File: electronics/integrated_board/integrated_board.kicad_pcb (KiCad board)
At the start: 2 copper layers, 54 parts, among them CON1 BARREL_JACK, J1 Conn_01x04_Female, J13 Conn_01x05_Female, J15 Conn_01x05_Female, J17 Conn_01x05_Female, J2 Conn_01x04_Female, J3 Conn_01x04_Female, P10 Conn_01x02, P15 Conn_01x02, P16 UART, P2 A1, P3 A2, P4 A3, P5 I2C 2, U3 LM2596T-5, U4 ESP32-DEVKITC-32D, U5 ULN2003, U6 ULN2003

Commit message: update integrated board
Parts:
- removed C10: 22nF, Capacitor_THT:CP_Radial_D4.0mm_P2.00mm
- removed J3: Conn_01x04_Female, Connector_JST:JST_XH_B4B-XH-A_1x04_P2.50mm_Vertical
- removed P5: I2C 2, Connector_JST:JST_XH_B4B-XH-A_1x04_P2.50mm_Vertical
- removed R16, R17: 1k, Resistor_THT:R_Axial_DIN0309_L9.0mm_D3.2mm_P12.70mm_Horizontal
- removed R18, R19: 1.8k, Resistor_THT:R_Axial_DIN0309_L9.0mm_D3.2mm_P12.70mm_Horizontal
- removed U5, U6: ULN2003, Package_DIP:DIP-16_W7.62mm_Socket_LongPads
- added C13: 22nF, Capacitor_THT:CP_Radial_D4.0mm_P2.00mm, F.Cu at (170.1, 106.8)
- added J5: to_rotary_encoder2 (14,27), Connector_JST:JST_XH_B4B-XH-A_1x04_P2.50mm_Vertical, F.Cu at (188.7, 100.5)
- added P1: Conn_01x02, Connector_JST:JST_XH_B2B-XH-A_1x02_P2.50mm_Vertical, F.Cu at (110.7, 49.8)
- added P6: io, Connector_JST:JST_XH_B4B-XH-A_1x04_P2.50mm_Vertical, F.Cu at (98.2, 130.8)
- added Q1: 2N7000, Package_TO_SOT_THT:TO-92_Inline_Wide, F.Cu at (163.4, 49.7)
- added Q2: 2N7000, Package_TO_SOT_THT:TO-92_Inline_Wide, F.Cu at (163.6, 67.3)
- added Q3: 2N7000, Package_TO_SOT_THT:TO-92_Inline_Wide, F.Cu at (163.4, 137.8)
- added Q4: 2N7000, Package_TO_SOT_THT:TO-92_Inline_Wide, F.Cu at (163.4, 120.4)
- added Q5: 2N7000, Package_TO_SOT_THT:TO-92_Inline_Wide, F.Cu at (163.7, 103.0)
- added Q6: 2N7000, Package_TO_SOT_THT:TO-92_Inline_Wide, F.Cu at (163.8, 85.0)
- added R28: 1k, Resistor_THT:R_Axial_DIN0309_L9.0mm_D3.2mm_P12.70mm_Horizontal, F.Cu at (179.9, 111.5)
- added R29: 1k, Resistor_THT:R_Axial_DIN0411_L9.9mm_D3.6mm_P12.70mm_Horizontal, F.Cu at (175.8, 111.5)
- added R30: 1k, Resistor_THT:R_Axial_DIN0411_L9.9mm_D3.6mm_P12.70mm_Horizontal, F.Cu at (175.8, 99.3)
- added R31: 1k, Resistor_THT:R_Axial_DIN0309_L9.0mm_D3.2mm_P12.70mm_Horizontal, F.Cu at (179.9, 81.7)
- added U1: ULN2003, Package_DIP:DIP-16_W7.62mm_LongPads, F.Cu at (123.0, 102.8)
- added U2: ULN2003, Package_DIP:DIP-16_W7.62mm_LongPads, F.Cu at (123.0, 80.4)
- C3, C4: value 22nF -> C_Small; footprint Capacitor_THT:CP_Radial_D4.0mm_P2.00mm -> Capacitor_THT:C_Disc_D6.0mm_W4.4mm_P5.00mm
- C7, C8: value C_Small -> 22nF; footprint Capacitor_THT:C_Disc_D6.0mm_W4.4mm_P5.00mm -> Capacitor_THT:CP_Radial_D4.0mm_P2.00mm
- J1: value Conn_01x04_Female -> to_rotary_encoder3(12,13)
- J13: value Conn_01x05_Female -> to_motor1(2,15,16,17)
- J15: value Conn_01x05_Female -> to_motor2 (5,18,19,21)
- J17: value Conn_01x05_Female -> to_motor3 (22,23,9,10)
- J2: value Conn_01x04_Female -> to_rotary_encoder3
- P2: value A1 -> io
- P4: value A3 -> io
- R1, R10, R11, R2, R3, R4, R8, R9: footprint Resistor_THT:R_Axial_DIN0309_L9.0mm_D3.2mm_P12.70mm_Horizontal -> Resistor_THT:R_Axial_DIN0411_L9.9mm_D3.6mm_P12.70mm_Horizontal
- R12, R13: value 1.8k -> 1k; footprint Resistor_THT:R_Axial_DIN0309_L9.0mm_D3.2mm_P12.70mm_Horizontal -> Resistor_THT:R_Axial_DIN0411_L9.9mm_D3.6mm_P12.70mm_Horizontal
- R5, R6: value 1.8k -> 1k
- moved P3 180.4 mm to (117.2, 130.8), turned to -90 degrees
- moved P4 172.3 mm to (117.2, 116.2), turned to -90 degrees
- moved P2 167.1 mm to (107.5, 130.8), turned to -90 degrees
- moved C9 165.6 mm to (170.3, 123.3), turned to 90 degrees
- moved C1 163.8 mm to (170.4, 53.0), turned to 90 degrees
- moved C2 162.9 mm to (170.4, 71.0), turned to 90 degrees
- moved J1 161.4 mm to (188.7, 66.0), turned to 90 degrees
- moved R5 155.1 mm to (179.7, 46.3), turned to -90 degrees
- moved J2 153.9 mm to (188.7, 137.0), turned to 90 degrees
- moved R6 150.6 mm to (179.7, 76.7), turned to 90 degrees
- moved R15 150.4 mm to (179.7, 117.3), turned to -90 degrees
- moved R14 150.3 mm to (179.7, 134.3), turned to -90 degrees
- moved H1 149.5 mm to (189.2, 45.5)
- moved R12 149.4 mm to (175.7, 146.7), turned to 180 degrees
- moved R10 148.7 mm to (175.6, 134.2), turned to 180 degrees
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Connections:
- C1 pad 1: GND -> Net-(J1-Pin_2)
- C1 pad 2: Net-(J1-Pin_1) -> GND
- C2 pad 1: GND -> Net-(J1-Pin_1)
- C2 pad 2: Net-(J1-Pin_2) -> GND
- C3 pad 2: Net-(J2-Pin_1) -> +5V
- C4 pad 2: Net-(J2-Pin_2) -> +5V
- C5 pad 1: Net-(P10-Pin_1) -> Net-(P1-Pin_2)
- C7 pad 1: GND -> Net-(J5-Pin_2)
- C7 pad 2: +5V -> GND
- C8 pad 1: GND -> Net-(J2-Pin_1)
- C8 pad 2: +5V -> GND
- C9 pad 1: GND -> Net-(J2-Pin_2)
- C9 pad 2: Net-(J3-Pin_1) -> GND
- CON1 pad 1: Net-(P10-Pin_1) -> Net-(P1-Pin_1)
- P10 pad 1: Net-(P10-Pin_1) -> Net-(P1-Pin_2)
- P15 pad 1: Net-(P10-Pin_1) -> Net-(P1-Pin_2)
- P2 pad 1: A1-3 -> Net-(P2-Pin_1)
- P2 pad 2: A1-4 -> Net-(P2-Pin_2)
- P4 pad 1: A3-3 -> Net-(P4-Pin_1)
- P4 pad 2: A3-4 -> Net-(P4-Pin_2)
- R1 pad 1: Net-(J1-Pin_1) -> +3V3
- R1 pad 2: +5V -> Net-(Q1-S)
- R10 pad 1: D5-3 -> +3V3
- R10 pad 2: Net-(J2-Pin_1) -> Net-(Q3-S)
- R11 pad 1: D5-4 -> +3V3
- R11 pad 2: Net-(J2-Pin_2) -> Net-(Q4-S)
- R12 pad 1: GND -> +5V
- R12 pad 2: D5-3 -> Net-(J2-Pin_1)
- R13 pad 1: GND -> +5V
- R13 pad 2: D5-4 -> Net-(J2-Pin_2)
- R14 pad 1: Net-(J3-Pin_1) -> Net-(J2-Pin_1)
- R15 pad 1: Net-(J3-Pin_2) -> +5V
- R15 pad 2: +5V -> Net-(J2-Pin_2)
- R2 pad 1: Net-(J1-Pin_2) -> +3V3
- R2 pad 2: +5V -> Net-(Q2-S)
- R3 pad 1: D1-3 -> +5V
- R3 pad 2: Net-(J1-Pin_1) -> Net-(J1-Pin_2)
- R4 pad 1: D1-4 -> +5V
- R4 pad 2: Net-(J1-Pin_2) -> Net-(J1-Pin_1)
- R5 pad 1: GND -> Net-(J1-Pin_2)
- R5 pad 2: D1-3 -> +5V
- R6 pad 1: GND -> +5V
- R6 pad 2: D1-4 -> Net-(J1-Pin_1)
- R7 pad 2: Net-(P10-Pin_1) -> Net-(P1-Pin_2)
- R8 pad 1: Net-(J2-Pin_1) -> +3V3
- R8 pad 2: +5V -> Net-(Q6-S)
- R9 pad 1: Net-(J2-Pin_2) -> +5V
- R9 pad 2: +5V -> Net-(J5-Pin_2)
- U3 pad 1: Net-(P10-Pin_1) -> Net-(P1-Pin_2)
- U4 pad 1: unconnected-(U4-3V3-Pad1) -> +3V3
- U4 pad 10: D8-3 -> Net-(Q4-S)
- U4 pad 11: D7-4 -> Net-(Q5-S)
- U4 pad 12: D7-3 -> Net-(Q6-S)
- U4 pad 13: I2C_2-3 -> Net-(Q2-S)
- U4 pad 15: I2C_2-4 -> Net-(Q1-S)
- U4 pad 16: I2C_1-3 -> to_uln2003_2
- U4 pad 17: I2C_1-4 -> to_uln2003_1
- U4 pad 21: D6-4 -> Net-(U1-I5)
- U4 pad 22: D6-3 -> Net-(U1-I6)
- U4 pad 25: D5-4 -> Net-(U1-I7)
- U4 pad 27: D5-3 -> Net-(U2-I1)
- U4 pad 28: D4-4 -> Net-(U2-I2)
- U4 pad 29: D4-3 -> Net-(U2-I3)
- U4 pad 30: D3-4 -> Net-(U2-I4)
- U4 pad 31: D3-3 -> Net-(U2-I5)
- U4 pad 32: D2-4 -> Net-(P6-Pin_1)
- U4 pad 33: D2-3 -> Net-(P6-Pin_2)
- U4 pad 34: D1-4 -> Net-(U2-I6)
- U4 pad 35: D1-3 -> Net-(U2-I7)
- U4 pad 5: A1-4 -> Net-(P4-Pin_2)
- U4 pad 6: A1-3 -> Net-(P4-Pin_1)
- U4 pad 7: A3-3 -> Net-(P2-Pin_2)
- U4 pad 8: A3-4 -> Net-(P2-Pin_1)
- U4 pad 9: D8-4 -> Net-(Q3-S)
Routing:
- net +5V: track 0.00 -> 571.4 mm
- net +3V3: track 0.00 -> 219.7 mm
- net Net-(P1-Pin_2): track 0.00 -> 177.9 mm
- net Net-(P6-Pin_2): track 0.00 -> 99.1 mm
- net Net-(P6-Pin_1): track 0.00 -> 93.8 mm
- net Net-(P2-Pin_2): track 0.00 -> 82.3 mm
- net Net-(P2-Pin_1): track 0.00 -> 81.3 mm
- net Net-(Q3-S): track 0.00 -> 72.0 mm
- net A2-4: track 0.00 -> 69.5 mm
- net A2-3: track 0.00 -> 68.6 mm
- net to_uln2003_1: track 0.00 -> 66.9 mm
- net to_uln2003_2: track 0.00 -> 65.9 mm
- net RX: track 0.00 -> 63.8 mm
- net TX: track 0.00 -> 59.9 mm
- net Net-(P4-Pin_2): track 0.00 -> 58.1 mm
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- added copper zone on B.Cu, net GND
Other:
- board outline added: 98.5 x 111 mm
- board text added: "12V"
- board text added: "12V conn"
- board text added: "Antenna side"
- board text added: "GND"
- board text added: "IO0"
- board text added: "IO34"
- board text added: "IO35"
- board text added: "IO36"
- board text added: "IO39"
- board text added: "IO4"
- board text added: "RX"
- board text added: "TX"
- board text added: "USB side"
- board text added: "VCC"
- board text added: "based on BeeHive v0.7"
- board text added: "board by Andre Maia Chagas licensed under CERN-OHL-W 2.0 https://ohwr.org/project/cernohl"

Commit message: update integrated board
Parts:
- removed P3: A2, Connector_JST:JST_XH_B4B-XH-A_1x04_P2.50mm_Vertical
- removed P6: io, Connector_JST:JST_XH_B4B-XH-A_1x04_P2.50mm_Vertical
- added R16: 10k, Resistor_THT:R_Axial_DIN0411_L9.9mm_D3.6mm_P12.70mm_Horizontal, F.Cu at (63.8, 75.8)
- added R17: 10k, Resistor_THT:R_Axial_DIN0411_L9.9mm_D3.6mm_P12.70mm_Horizontal, F.Cu at (63.8, 80.9)
- added R18: 1k, Resistor_THT:R_Axial_DIN0411_L9.9mm_D3.6mm_P12.70mm_Horizontal, F.Cu at (63.8, 86.0)
- added R19: 1k, Resistor_THT:R_Axial_DIN0411_L9.9mm_D3.6mm_P12.70mm_Horizontal, F.Cu at (63.8, 91.2)
- added R20: 1k, Resistor_THT:R_Axial_DIN0411_L9.9mm_D3.6mm_P12.70mm_Horizontal, F.Cu at (63.8, 96.3)
- added R21: 1k, Resistor_THT:R_Axial_DIN0411_L9.9mm_D3.6mm_P12.70mm_Horizontal, F.Cu at (63.8, 101.5)
- added SW1: SW_Push, Connector_JST:JST_XH_B2B-XH-A_1x02_P2.50mm_Vertical, F.Cu at (82.0, 76.5)
- added SW2: SW_Push, Connector_JST:JST_XH_B2B-XH-A_1x02_P2.50mm_Vertical, F.Cu at (82.0, 84.3)
- J13: value to_motor1(2,15,16,17) -> to_motor1(15,2,0,4)
- J15: value to_motor2 (5,18,19,21) -> to_motor2 (16,17,5,18)
- J17: value to_motor3 (22,23,9,10) -> to_motor3 (19,21,22,23)
- P2: value io -> LCD
- moved P2 9.20 mm to (98.2, 130.8)
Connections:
- net Net-(Q5-S) renamed encoderX_2
- net Net-(Q6-S) renamed encoderX_1
- Q1 pad 1: Net-(Q1-S) -> encoderZ_1
- Q2 pad 1: Net-(Q2-S) -> encoderZ_2
- Q3 pad 1: Net-(Q3-S) -> encoderY_1
- Q4 pad 1: Net-(Q4-S) -> encoderY_2
- R1 pad 2: Net-(Q1-S) -> encoderZ_1
- R10 pad 2: Net-(Q3-S) -> encoderY_1
- R11 pad 2: Net-(Q4-S) -> encoderY_2
- R2 pad 2: Net-(Q2-S) -> encoderZ_2
- U1 pad 3: to_uln2003_2 -> Net-(U1-I3)
- U1 pad 4: to_uln2003_1 -> Net-(U1-I4)
- U4 pad 10: Net-(Q4-S) -> encoderY_1
- U4 pad 13: Net-(Q2-S) -> Net-(P4-Pin_2)
- U4 pad 15: Net-(Q1-S) -> Net-(P4-Pin_1)
- U4 pad 16: to_uln2003_2 -> unconnected-(U4-SD2-Pad16)
- U4 pad 17: to_uln2003_1 -> unconnected-(U4-SD3-Pad17)
- U4 pad 21: Net-(U1-I5) -> Net-(U1-I3)
- U4 pad 22: Net-(U1-I6) -> Net-(U1-I4)
- U4 pad 25: Net-(U1-I7) -> Net-(U1-I5)
- U4 pad 27: Net-(U2-I1) -> Net-(U1-I6)
- U4 pad 28: Net-(U2-I2) -> Net-(U1-I7)
- U4 pad 29: Net-(U2-I3) -> Net-(U2-I1)
- U4 pad 3: A2-4 -> switch2
- U4 pad 30: Net-(U2-I4) -> Net-(U2-I2)
- U4 pad 31: Net-(U2-I5) -> Net-(U2-I3)
- U4 pad 32: Net-(P6-Pin_1) -> Net-(U2-I4)
- U4 pad 33: Net-(P6-Pin_2) -> Net-(U2-I5)
- U4 pad 4: A2-3 -> switch1
- U4 pad 5: Net-(P4-Pin_2) -> encoderZ_2
- U4 pad 6: Net-(P4-Pin_1) -> encoderZ_1
- U4 pad 9: Net-(Q3-S) -> encoderY_2
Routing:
- net (no net): track 0.00 -> 132.8 mm
- net Net-(P6-Pin_2): track 99.1 -> 0.00 mm
- net Net-(P6-Pin_1): track 93.8 -> 0.00 mm
- net Net-(Q3-S): track 72.0 -> 0.00 mm
- net A2-4: track 69.5 -> 0.00 mm
- net A2-3: track 68.6 -> 0.00 mm
- net to_uln2003_1: track 66.9 -> 0.00 mm
- net to_uln2003_2: track 65.9 -> 0.00 mm
- net Net-(Q4-S): track 56.6 -> 0.00 mm
- net switch1: track 0.00 -> 20.7 mm
- net switch2: track 0.00 -> 19.2 mm
- net Net-(Q1-S): track 16.1 -> 0.00 mm
- net Net-(U1-I7): track 13.5 -> 0.48 mm
- net Net-(Q2-S): track 12.7 -> 0.00 mm
- net Net-(U2-I3): track 11.3 -> 0.00 mm
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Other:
- board text removed: "IO36"
- board text removed: "IO39"

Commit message: finish revision of integrated pcb board, create production files
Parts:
- removed C13, C7: 22nF, Capacitor_THT:CP_Radial_D4.0mm_P2.00mm
- removed J5: to_rotary_encoder2 (14,27), Connector_JST:JST_XH_B4B-XH-A_1x04_P2.50mm_Vertical
- removed Q1, Q2, Q3, Q4, Q5, Q6: 2N7000, Package_TO_SOT_THT:TO-92_Inline_Wide
- removed R28, R31: 1k, Resistor_THT:R_Axial_DIN0309_L9.0mm_D3.2mm_P12.70mm_Horizontal
- removed R29, R30, R8, R9: 1k, Resistor_THT:R_Axial_DIN0411_L9.9mm_D3.6mm_P12.70mm_Horizontal
- added C10: 22nF, Capacitor_THT:C_Disc_D6.0mm_W4.4mm_P5.00mm, F.Cu at (180.4, 110.8)
- added C11: 22nF, Capacitor_THT:C_Disc_D6.0mm_W4.4mm_P5.00mm, F.Cu at (169.7, 124.4)
- added J3: to_rotary_encoderX(14,27), Connector_JST:JST_XH_B4B-XH-A_1x04_P2.50mm_Vertical, F.Cu at (187.4, 62.6)
- added R22: 1kΩ, Resistor_THT:R_Axial_DIN0309_L9.0mm_D3.2mm_P12.70mm_Horizontal, F.Cu at (177.9, 107.4)
- added R23: 1kΩ, Resistor_THT:R_Axial_DIN0309_L9.0mm_D3.2mm_P12.70mm_Horizontal, F.Cu at (162.7, 107.2)
- added R24: 1.8k, Resistor_THT:R_Axial_DIN0309_L9.0mm_D3.2mm_P12.70mm_Horizontal, F.Cu at (175.2, 111.4)
- added R25: 1kΩ, Resistor_THT:R_Axial_DIN0309_L9.0mm_D3.2mm_P12.70mm_Horizontal, F.Cu at (177.7, 119.6)
- added R26: 1kΩ, Resistor_THT:R_Axial_DIN0309_L9.0mm_D3.2mm_P12.70mm_Horizontal, F.Cu at (162.4, 119.6)
- added R27: 1.8k, Resistor_THT:R_Axial_DIN0309_L9.0mm_D3.2mm_P12.70mm_Horizontal, F.Cu at (175.2, 115.6)
- C1, C2, C8, C9: footprint Capacitor_THT:CP_Radial_D4.0mm_P2.00mm -> Capacitor_THT:C_Disc_D6.0mm_W4.4mm_P5.00mm
- J1: value to_rotary_encoder3(12,13) -> to_rotary_encoderZ(35,34)
- J13: value to_motor1(15,2,0,4) -> motor1(15,2,0,4)
- J15: value to_motor2 (16,17,5,18) -> motor2 (16,17,5,18)
- J17: value to_motor3 (19,21,22,23) -> motor3 (19,21,22,23)
- J2: value to_rotary_encoder3 -> to_rotary_encoderY(25,26)
- R1, R10, R11, R13, R2, R4: value 1k -> 1kΩ; footprint Resistor_THT:R_Axial_DIN0411_L9.9mm_D3.6mm_P12.70mm_Horizontal -> Resistor_THT:R_Axial_DIN0309_L9.0mm_D3.2mm_P12.70mm_Horizontal
- R12, R3: value 1k -> 1.8k; footprint Resistor_THT:R_Axial_DIN0411_L9.9mm_D3.6mm_P12.70mm_Horizontal -> Resistor_THT:R_Axial_DIN0309_L9.0mm_D3.2mm_P12.70mm_Horizontal
- R14, R5: value 1k -> 1kΩ
- R15, R6: value 1k -> 1.8k
- moved R13 87.4 mm to (177.0, 42.0), turned to -90 degrees
- moved R12 85.7 mm to (173.2, 61.0)
- moved R14 83.5 mm to (160.5, 53.0), turned to 0 degrees
- moved R16 79.9 mm to (115.2, 137.0)
- moved SW1 76.7 mm to (113.5, 146.5)
- moved C9 75.9 mm to (165.6, 47.6), turned to 0 degrees
- moved SW2 74.5 mm to (123.0, 146.5)
- moved R17 72.2 mm to (115.0, 131.8)
- moved C8 71.3 mm to (165.6, 69.8), turned to 0 degrees
- moved J1 70.0 mm to (188.4, 136.0)
- moved R21 68.7 mm to (127.8, 126.5), turned to 180 degrees
- moved R18 68.6 mm to (127.8, 111.0), turned to 180 degrees
- moved R20 68.6 mm to (127.8, 121.2), turned to 180 degrees
- moved R19 68.6 mm to (127.8, 116.0), turned to 180 degrees
- moved R10 63.8 mm to (177.0, 70.4), turned to 90 degrees
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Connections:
- C1 pad 1: Net-(J1-Pin_2) -> GND
- C1 pad 2: GND -> Net-(J2-Pin_1)
- C2 pad 1: Net-(J1-Pin_1) -> GND
- C2 pad 2: GND -> Net-(J2-Pin_2)
- C8 pad 1: Net-(J2-Pin_1) -> GND
- C8 pad 2: GND -> Net-(J3-Pin_1)
- C9 pad 1: Net-(J2-Pin_2) -> GND
- C9 pad 2: GND -> Net-(J3-Pin_2)
- R1 pad 1: +3V3 -> Net-(J2-Pin_1)
- R1 pad 2: encoderZ_1 -> +5V
- R10 pad 1: +3V3 -> Net-(J3-Pin_1)
- R10 pad 2: encoderY_1 -> +5V
- R11 pad 1: +3V3 -> encoderX_2
- R11 pad 2: encoderY_2 -> Net-(J3-Pin_1)
- R12 pad 1: +5V -> GND
- R12 pad 2: Net-(J2-Pin_1) -> encoderX_2
- R13 pad 1: +5V -> Net-(J3-Pin_2)
- R13 pad 2: Net-(J2-Pin_2) -> +5V
- R14 pad 1: Net-(J2-Pin_1) -> encoderX_1
- R14 pad 2: +5V -> Net-(J3-Pin_2)
- R15 pad 1: +5V -> GND
- R15 pad 2: Net-(J2-Pin_2) -> encoderX_1
- R2 pad 1: +3V3 -> encoderY_1
- R2 pad 2: encoderZ_2 -> Net-(J2-Pin_1)
- R3 pad 1: +5V -> GND
- R3 pad 2: Net-(J1-Pin_2) -> encoderY_1
- R4 pad 1: +5V -> Net-(J2-Pin_2)
- R4 pad 2: Net-(J1-Pin_1) -> +5V
- R5 pad 1: Net-(J1-Pin_2) -> encoderY_2
- R5 pad 2: +5V -> Net-(J2-Pin_2)
- R6 pad 1: +5V -> GND
- R6 pad 2: Net-(J1-Pin_1) -> encoderY_2
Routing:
- net +3V3: track 219.7 -> 0.00 mm
- net (no net): track 132.8 -> 0.00 mm
- net +5V: track 571.4 -> 481.0 mm
- net switch2: track 19.2 -> 86.4 mm
- net switch1: track 20.7 -> 87.4 mm
- net Net-(P4-Pin_1): track 56.9 -> 102.0 mm, vias 0 -> 1
- net Net-(R20-Pad1): track 0.00 -> 42.7 mm
- net Net-(P4-Pin_2): track 58.1 -> 98.7 mm, vias 0 -> 1
- net encoderZ_2: track 3.98 -> 44.3 mm
- net Net-(J5-Pin_1): track 37.1 -> 0.00 mm
- net Net-(J3-Pin_2): track 0.00 -> 36.1 mm
- net encoderZ_1: track 3.92 -> 38.0 mm
- net Net-(J5-Pin_2): track 33.6 -> 0.00 mm
- net encoderX_2: track 40.2 -> 8.66 mm
- net Net-(J3-Pin_1): track 0.00 -> 27.3 mm
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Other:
- board text added: "J1"
- board text added: "R11"
- board text added: "R24"

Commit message: fix board bugs
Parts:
- removed R20, R21: 1k, Resistor_THT:R_Axial_DIN0411_L9.9mm_D3.6mm_P12.70mm_Horizontal
- C3, C4: value C_Small -> 10µF
- J1: value to_rotary_encoderZ(35,34) -> rot_encoderZ(35,34)
- J2: value to_rotary_encoderY(25,26) -> rot_encoderY(25,26)
- J3: value to_rotary_encoderX(14,27) -> rot_encoderX(14,27)
- R16, R17: value 10k -> 1.8k
- moved P4 35.2 mm to (139.0, 146.5), turned to 0 degrees
- moved P10 24.0 mm to (162.5, 146.5)
- moved P15 24.0 mm to (173.8, 146.5)
- moved R16 16.3 mm to (127.8, 126.8), turned to 180 degrees
- moved R17 10.2 mm to (115.0, 121.5)
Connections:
- SW1 pad 2: Net-(R20-Pad1) -> Net-(R18-Pad2)
- SW2 pad 2: Net-(R21-Pad1) -> Net-(R18-Pad2)
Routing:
- net Net-(R18-Pad2): track 15.5 -> 63.6 mm
- net Net-(R20-Pad1): track 42.7 -> 0.00 mm
- net Net-(R21-Pad1): track 23.0 -> 0.00 mm
- net Net-(P4-Pin_1): track 102.0 -> 115.8 mm
- net Net-(P4-Pin_2): track 98.7 -> 111.6 mm
- net switch1: track 87.4 -> 90.1 mm
- net +5V: track 481.0 -> 482.7 mm
- net switch2: track 86.4 -> 85.4 mm
- net Net-(P1-Pin_2): track 177.8 -> 176.8 mm
- net Net-(J1-Pin_1): track 36.2 -> 35.6 mm
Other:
- board text added: "IO32"
- board text added: "IO33"
- board text removed: "IO0"
- board text removed: "IO4"

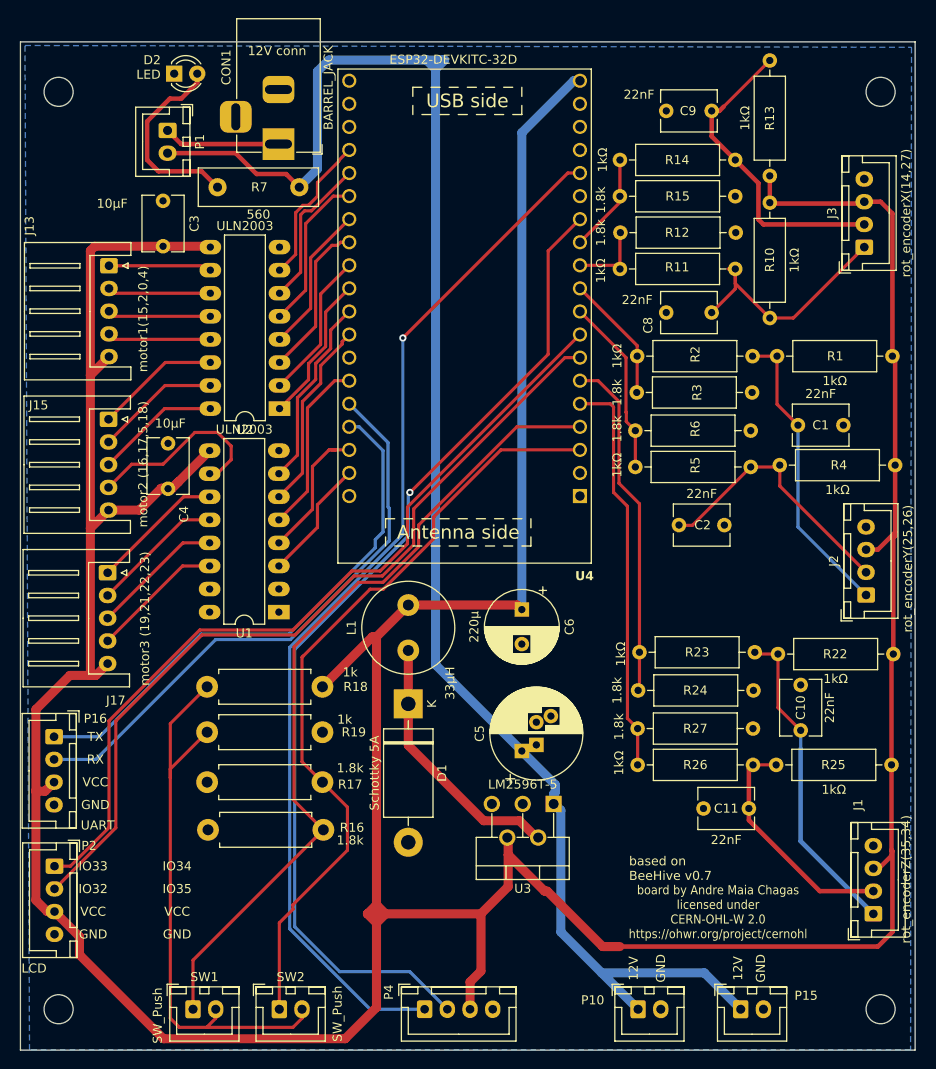
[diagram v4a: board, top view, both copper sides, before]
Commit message: Expanding integrated board
-Board now incorporates pcr8575 gpio expander
-removed UART port
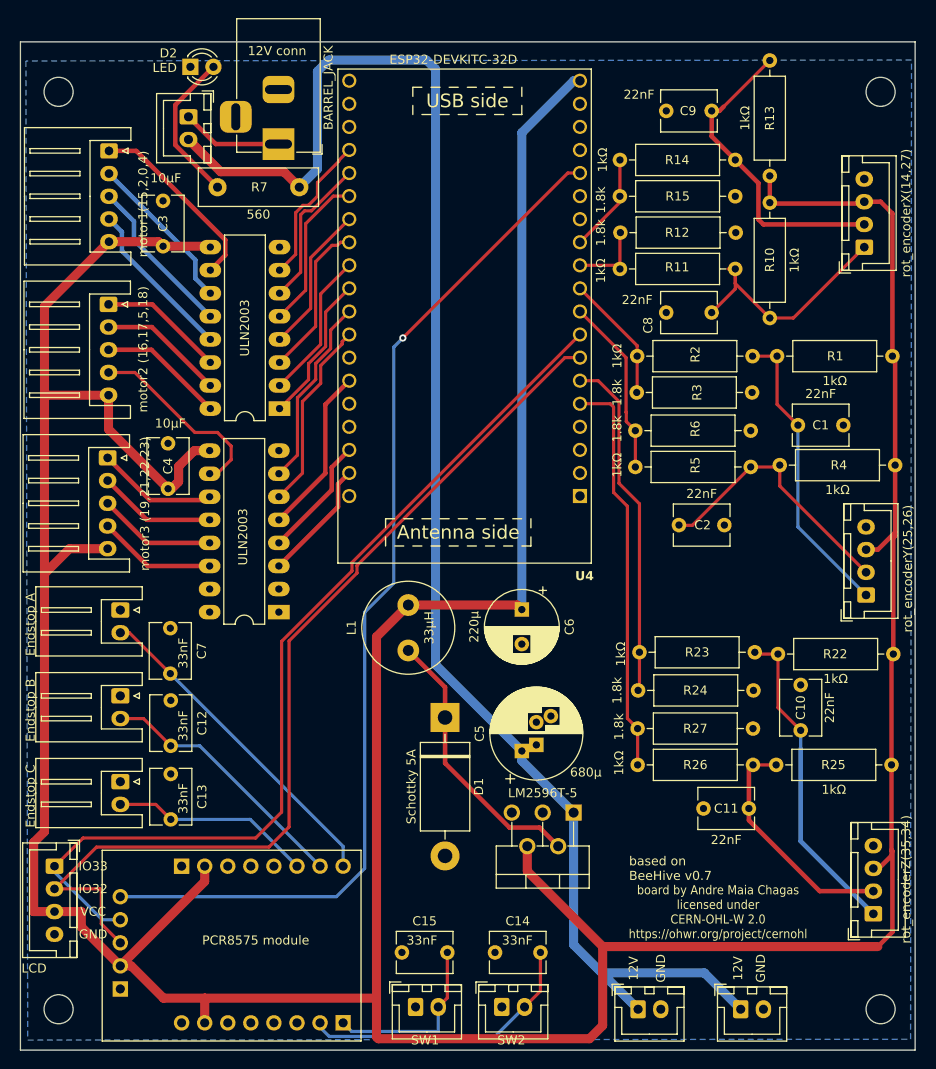
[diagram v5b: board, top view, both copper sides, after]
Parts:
- removed P16: UART, Connector_JST:JST_XH_B4B-XH-A_1x04_P2.50mm_Vertical
- removed P4: io, Connector_JST:JST_XH_B4B-XH-A_1x04_P2.50mm_Vertical
- removed R16, R17: 1.8k, Resistor_THT:R_Axial_DIN0411_L9.9mm_D3.6mm_P12.70mm_Horizontal
- removed R18, R19: 1k, Resistor_THT:R_Axial_DIN0411_L9.9mm_D3.6mm_P12.70mm_Horizontal
- removed SW1, SW2: SW_Push, Connector_JST:JST_XH_B2B-XH-A_1x02_P2.50mm_Vertical
- added C12: C, Capacitor_THT:C_Disc_D6.0mm_W4.4mm_P5.00mm, F.Cu at (111.0, 112.5)
- added C13: C, Capacitor_THT:C_Disc_D6.0mm_W4.4mm_P5.00mm, F.Cu at (111.0, 120.6)
- added C14: C, Capacitor_THT:C_Disc_D6.0mm_W4.4mm_P5.00mm, F.Cu at (146.8, 140.2)
- added C15: C, Capacitor_THT:C_Disc_D6.0mm_W4.4mm_P5.00mm, F.Cu at (136.5, 140.2)
- added C7: C, Capacitor_THT:C_Disc_D6.0mm_W4.4mm_P5.00mm, F.Cu at (111.0, 104.5)
- added J10: pcf8575 IO expander, Connector_PinHeader_2.54mm:PinHeader_1x05_P2.54mm_Vertical, B.Cu at (105.5, 144.3)
- added J11: Switch 1, Connector_JST:JST_XH_B2B-XH-A_1x02_P2.50mm_Vertical, F.Cu at (138.0, 146.2)
- added J4: Switch 2, Connector_JST:JST_XH_B2B-XH-A_1x02_P2.50mm_Vertical, F.Cu at (147.5, 146.2)
- added J5: Endstop A, Connector_JST:JST_XH_S2B-XH-A_1x02_P2.50mm_Horizontal, F.Cu at (105.5, 102.5)
- added J6: Endstop B, Connector_JST:JST_XH_S2B-XH-A_1x02_P2.50mm_Horizontal, F.Cu at (105.5, 112.0)
- added J7: Endstop C, Connector_JST:JST_XH_S2B-XH-A_1x02_P2.50mm_Horizontal, F.Cu at (105.5, 121.5)
- added J8: Conn_01x16, Connector_PinHeader_2.54mm:PinHeader_1x08_P2.54mm_Vertical, B.Cu at (130.0, 148.0)
- added J9: Conn_01x16, Connector_PinHeader_2.54mm:PinHeader_1x08_P2.54mm_Vertical, B.Cu at (112.2, 130.8)
- moved J13 12.7 mm to (104.2, 52.0)
- moved J17 12.7 mm to (104.1, 85.8)
- moved J15 12.6 mm to (104.2, 68.9)
- moved D1 4.32 mm to (141.2, 114.4)
- moved P1 2.75 mm to (113.0, 48.2)
- moved U3 2.40 mm to (155.4, 124.8)
- moved D2 1.94 mm to (113.2, 42.8)
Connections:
- U4 pad 13: Net-(P4-Pin_2) -> unconnected-(U4-IO12-Pad13)
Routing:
- net Net-(P4-Pin_2): track 111.6 -> 0.00 mm, vias 1 -> 0
- net switch1: track 90.1 -> 0.00 mm
- net switch2: track 85.4 -> 0.00 mm
- net RX: track 63.8 -> 0.00 mm
- net Net-(R18-Pad2): track 63.6 -> 0.00 mm
- net TX: track 59.9 -> 0.00 mm
- net Net-(J5-Pin_2): track 0.00 -> 36.4 mm
- net Net-(J4-Pin_2): track 0.00 -> 31.5 mm
- net Net-(J6-Pin_2): track 0.00 -> 28.7 mm
- net Net-(J7-Pin_2): track 0.00 -> 22.3 mm
- net Net-(J11-Pin_2): track 0.00 -> 20.0 mm
- net Net-(J10-Pin_3): track 91.2 -> 106.4 mm
- net Net-(J10-Pin_4): track 91.3 -> 103.7 mm
- net +5V: track 482.7 -> 493.9 mm
- net Net-(J13-Pin_1): track 10.7 -> 20.9 mm
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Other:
- board text added: "33nF"
- board text added: "680μ"
- board text added: "Endstop A"
- board text added: "Endstop B"
- board text added: "Endstop C"
- board text added: "PCR8575 module"
- board text added: "SW1"
- board text added: "SW2"
- board text removed: "IO34"
- board text removed: "IO35"
- board text removed: "RX"
- board text removed: "TX"
